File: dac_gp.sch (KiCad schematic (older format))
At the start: 7 parts, among them U17 MAX5802

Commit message: cleanup from Eagle import
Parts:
- C52, C53: footprint adc_dac_v1:C0603 -> Capacitor_SMD:C_0603_1608Metric; symbol adc_dac_v1-eagle-import:C-USC0603 -> Device:C
- R33, R34, R35, R36: footprint adc_dac_v1:R0603 -> Resistor_SMD:R_0603_1608Metric; symbol adc_dac_v1-eagle-import:R-US_R0603 -> Device:R_US
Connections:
- net labels added: +3V3, +5V
- net labels removed: 3V3, 5V
- wire segments 21 -> 25
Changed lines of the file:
@@
 $Descr User 12505 8268
 encoding utf-8
-Sheet 12 14
+Sheet 6 8
 Title ""
 Date ""
@@
 Comment4 ""
 $EndDescr
-Wire Wire Line
-	6000 2500 5500 2500
-Text GLabel 5500 2500 2    70   BiDi ~ 0
-3V3
-Wire Wire Line
-	4200 2400 4200 2200
-Wire Wire Line
-	4200 2200 4500 2200
-Wire Wire Line
-	4500 2200 4800 2200
-Wire Wire Line
-	4500 2300 4500 2200
-Connection ~ 4500 2200
-Text GLabel 4200 2200 2    70   BiDi ~ 0
-3V3
-Wire Wire Line
-	5000 1500 5000 1300
-Text GLabel 5000 1400 2    70   BiDi ~ 0
-3V3
-Wire Wire Line
-	6000 2300 5500 2300
-Text GLabel 5500 2300 2    70   BiDi ~ 0
-5V_REF
-Wire Wire Line
-	7900 2700 8200 2700
-Wire Wire Line
-	8200 2700 8200 2900
-Text GLabel 7900 2700 0    10   BiDi ~ 0
-GND
-Wire Wire Line
-	5800 3500 5800 3400
-Text GLabel 5800 3500 0    10   BiDi ~ 0
-GND
-Wire Wire Line
-	5000 1800 5000 1900
-Text GLabel 5000 1800 0    10   BiDi ~ 0
-GND
-Wire Wire Line
-	5400 1900 5400 1800
-Text GLabel 5400 1900 0    10   BiDi ~ 0
-GND
-Wire Wire Line
-	6000 2400 5500 2400
-Text GLabel 5500 2400 2    70   BiDi ~ 0
-5V
-Wire Wire Line
-	5400 1300 5400 1500
-Text GLabel 5400 1400 2    70   BiDi ~ 0
-5V
-Wire Wire Line
-	7900 2300 8300 2300
-Text GLabel 8000 2300 2    70   BiDi ~ 0
-DS_OUT0
-Wire Wire Line
-	7900 2400 8300 2400
-Text GLabel 8000 2400 2    70   BiDi ~ 0
-DS_OUT1
-Wire Wire Line
-	4800 2600 6000 2600
-Text GLabel 5500 2600 2    70   BiDi ~ 0
-DS_SDA
-Wire Wire Line
-	4500 2700 6000 2700
-Text GLabel 5500 2700 2    70   BiDi ~ 0
-DS_SCL
-Wire Wire Line
-	6000 2800 4200 2800
-Text GLabel 5400 2800 2    70   BiDi ~ 0
-DS_CLRB
-Wire Wire Line
-	5800 3000 5800 2900
-Wire Wire Line
-	5800 2900 6000 2900
 $Comp
 L adc_dac_v1-eagle-import:FRAME_A_L #FRAME7
@@
 $EndComp
 $Comp
-L adc_dac_v1-eagle-import:FRAME_A_L #FRAME7
-U 2 1 519C2D19
-P 7700 6900
-F 0 "#FRAME7" H 7700 6900 50  0001 C CNN
-F 1 "FRAME_A_L" H 7700 6900 50  0001 C CNN
-F 2 "" H 7700 6900 50  0001 C CNN
-F 3 "" H 7700 6900 50  0001 C CNN
-	2    7700 6900
-	1    0    0    -1
-$EndComp
-$Comp
-L adc_dac_v1-eagle-import:GND #GND63
+L power:GND #GND063
 U 1 1 E9B71633
 P 8200 3000
-F 0 "#GND63" H 8200 3000 50  0001 C CNN
+F 0 "#GND063" H 8200 3000 50  0001 C CNN
 F 1 "GND" H 8100 2900 59  0000 L BNN
 F 2 "" H 8200 3000 50  0001 C CNN
@@
 $EndComp
 $Comp
-L adc_dac_v1-eagle-import:R-US_R0603 R33
+L Device:R_US R33
 U 1 1 FACA8B8B
 P 4800 2400
 F 0 "R33" H 4650 2459 59  0000 L BNN
 F 1 "4.7k" H 4650 2270 59  0000 L BNN
-F 2 "adc_dac_v1:R0603" H 4800 2400 50  0001 C CNN
+F 2 "Resistor_SMD:R_0603_1608Metric" H 4800 2400 50  0001 C CNN
 F 3 "" H 4800 2400 50  0001 C CNN
 	1    4800 2400
-	0    -1   -1   0
-$EndComp
-$Comp
-L adc_dac_v1-eagle-import:R-US_R0603 R34
+	1    0    0    -1
+$EndComp
+$Comp
+L Device:R_US R34
 U 1 1 24585AD3
 P 4500 2500
 F 0 "R34" H 4350 2559 59  0000 L BNN
 F 1 "4.7k" H 4350 2370 59  0000 L BNN
-F 2 "adc_dac_v1:R0603" H 4500 2500 50  0001 C CNN
+F 2 "Resistor_SMD:R_0603_1608Metric" H 4500 2500 50  0001 C CNN
 F 3 "" H 4500 2500 50  0001 C CNN
 	1    4500 2500
-	0    -1   -1   0
-$EndComp
-$Comp
-L adc_dac_v1-eagle-import:R-US_R0603 R35
+	1    0    0    -1
+$EndComp
+$Comp
+L Device:R_US R35
 U 1 1 8E3E5586
 P 4200 2600
 F 0 "R35" H 4050 2659 59  0000 L BNN
 F 1 "100k" H 4050 2470 59  0000 L BNN
-F 2 "adc_dac_v1:R0603" H 4200 2600 50  0001 C CNN
+F 2 "Resistor_SMD:R_0603_1608Metric" H 4200 2600 50  0001 C CNN
 F 3 "" H 4200 2600 50  0001 C CNN
 	1    4200 2600
-	0    -1   -1   0
-$EndComp
-$Comp
-L adc_dac_v1-eagle-import:R-US_R0603 R36
+	1    0    0    -1
+$EndComp
+$Comp
+L Device:R_US R36
 U 1 1 610F8BED
 P 5800 3200
 F 0 "R36" H 5650 3259 59  0000 L BNN
 F 1 "100k" H 5650 3070 59  0000 L BNN
-F 2 "adc_dac_v1:R0603" H 5800 3200 50  0001 C CNN
+F 2 "Resistor_SMD:R_0603_1608Metric" H 5800 3200 50  0001 C CNN
 F 3 "" H 5800 3200 50  0001 C CNN
 	1    5800 3200
-	0    -1   -1   0
-$EndComp
-$Comp
-L adc_dac_v1-eagle-import:GND #GND64
+	1    0    0    -1
+$EndComp
+$Comp
+L power:GND #GND064
 U 1 1 C02F8759
 P 5800 3600
-F 0 "#GND64" H 5800 3600 50  0001 C CNN
+F 0 "#GND064" H 5800 3600 50  0001 C CNN
 F 1 "GND" H 5700 3500 59  0000 L BNN
 F 2 "" H 5800 3600 50  0001 C CNN
@@
 $EndComp
 $Comp
-L adc_dac_v1-eagle-import:C-USC0603 C52
+L Device:C C52
 U 1 1 A7A1DCDA
-P 5000 1600
-F 0 "C52" H 5040 1625 59  0000 L BNN
-F 1 "0.1u" H 5040 1435 59  0000 L BNN
-F 2 "adc_dac_v1:C0603" H 5000 1600 50  0001 C CNN
-F 3 "" H 5000 1600 50  0001 C CNN
-	1    5000 1600
-	1    0    0    -1
-$EndComp
-$Comp
-L adc_dac_v1-eagle-import:C-USC0603 C53
+P 5000 1700
+F 0 "C52" H 5040 1725 59  0000 L BNN
+F 1 "0.1u" H 5040 1535 59  0000 L BNN
+F 2 "Capacitor_SMD:C_0603_1608Metric" H 5000 1700 50  0001 C CNN
+F 3 "" H 5000 1700 50  0001 C CNN
+	1    5000 1700
+	1    0    0    -1
+$EndComp
+$Comp
+L Device:C C53
 U 1 1 46ACB443
-P 5400 1600
-F 0 "C53" H 5440 1625 59  0000 L BNN
-F 1 "0.1u" H 5440 1435 59  0000 L BNN
-F 2 "adc_dac_v1:C0603" H 5400 1600 50  0001 C CNN
-F 3 "" H 5400 1600 50  0001 C CNN
-	1    5400 1600
-	1    0    0    -1
-$EndComp
-$Comp
-L adc_dac_v1-eagle-import:GND #GND62
+P 5400 1650
+F 0 "C53" H 5440 1675 59  0000 L BNN
+F 1 "0.1u" H 5440 1485 59  0000 L BNN
+F 2 "Capacitor_SMD:C_0603_1608Metric" H 5400 1650 50  0001 C CNN
+F 3 "" H 5400 1650 50  0001 C CNN
+	1    5400 1650
+	1    0    0    -1
+$EndComp
+$Comp
+L power:GND #GND062
 U 1 1 FC55E54D
 P 5000 2000
-F 0 "#GND62" H 5000 2000 50  0001 C CNN
+F 0 "#GND062" H 5000 2000 50  0001 C CNN
 F 1 "GND" H 4900 1900 59  0000 L BNN
 F 2 "" H 5000 2000 50  0001 C CNN
@@
 $EndComp
 $Comp
-L adc_dac_v1-eagle-import:GND #GND80
+L power:GND #GND080
 U 1 1 10B103BF
 P 5400 2000
-F 0 "#GND80" H 5400 2000 50  0001 C CNN
+F 0 "#GND080" H 5400 2000 50  0001 C CNN
 F 1 "GND" H 5300 1900 59  0000 L BNN
 F 2 "" H 5400 2000 50  0001 C CNN
@@
 	1    0    0    -1
 $EndComp
+Text GLabel 5500 2300 2    70   BiDi ~ 0
+5V_REF
+Text GLabel 8150 2300 2    70   BiDi ~ 0
+DS_OUT0
+Text GLabel 8150 2400 2    70   BiDi ~ 0
+DS_OUT1
+Text GLabel 5500 2600 2    70   BiDi ~ 0
+DS_SDA
+Text GLabel 5500 2700 2    70   BiDi ~ 0
+DS_SCL
+Text GLabel 5400 2800 2    70   BiDi ~ 0
+DS_CLRB
 Text Notes 6300 3200 0    59   ~ 0
 Slow DAC for offset voltages, etc.
+Wire Wire Line
+	6000 2500 5500 2500
+Wire Wire Line
+	4500 2200 4800 2200
+Wire Wire Line
+	6000 2300 5500 2300
+Wire Wire Line
+	7900 2700 8200 2700
+Wire Wire Line
+	6000 2400 5500 2400
+Wire Wire Line
+	5400 1300 5400 1500
+Wire Wire Line
+	7900 2300 8150 2300
+Wire Wire Line
+	7900 2400 8150 2400
+Wire Wire Line
+	4800 2600 6000 2600
+Wire Wire Line
+	4500 2700 6000 2700
+Wire Wire Line
+	6000 2800 4200 2800
+Wire Wire Line
+	5800 2900 6000 2900
+Connection ~ 4500 2200
+Wire Wire Line
+	5400 1800 5400 2000
+Wire Wire Line
+	5800 2900 5800 3050
+Wire Wire Line
+	5800 3350 5800 3600
+Wire Wire Line
+	4200 2800 4200 2750
+Wire Wire Line
+	4200 2200 4200 2450
+Wire Wire Line
+	4500 2200 4500 2350
+Wire Wire Line
+	4500 2650 4500 2700
+Wire Wire Line
+	4800 2600 4800 2550
+Wire Wire Line
+	4800 2250 4800 2200
+Wire Wire Line
+	5000 1350 5000 1550
+Wire Wire Line
+	5000 2000 5000 1850
+Wire Wire Line
+	8200 2700 8200 3000
+$Comp
+L power:+5V #PWR0123
+U 1 1 61889133
+P 5400 1300
+F 0 "#PWR0123" H 5400 1150 50  0001 C CNN
+F 1 "+5V" H 5415 1473 50  0000 C CNN
+F 2 "" H 5400 1300 50  0001 C CNN
+F 3 "" H 5400 1300 50  0001 C CNN
+	1    5400 1300
+	1    0    0    -1
+$EndComp
+$Comp
+L power:+5V #PWR0124
+U 1 1 6188A365
+P 5500 2400
+F 0 "#PWR0124" H 5500 2250 50  0001 C CNN
+F 1 "+5V" V 5515 2528 50  0000 L CNN
+F 2 "" H 5500 2400 50  0001 C CNN
+F 3 "" H 5500 2400 50  0001 C CNN
+	1    5500 2400
+	0    -1   -1   0
+$EndComp
+$Comp
+L power:+3V3 #PWR0125
+U 1 1 6188B164
+P 5000 1350
+F 0 "#PWR0125" H 5000 1200 50  0001 C CNN
+F 1 "+3V3" H 5015 1523 50  0000 C CNN
+F 2 "" H 5000 1350 50  0001 C CNN
+F 3 "" H 5000 1350 50  0001 C CNN
+	1    5000 1350
+	1    0    0    -1
+$EndComp
+$Comp
+L power:+3V3 #PWR0126
+U 1 1 6188C0A8
+P 4500 2200
+F 0 "#PWR0126" H 4500 2050 50  0001 C CNN
+F 1 "+3V3" H 4515 2373 50  0000 C CNN
+F 2 "" H 4500 2200 50  0001 C CNN
+F 3 "" H 4500 2200 50  0001 C CNN
+	1    4500 2200
+	1    0    0    -1
+$EndComp
+$Comp
+L power:+3V3 #PWR0127
+U 1 1 6188C619
+P 5500 2500
+F 0 "#PWR0127" H 5500 2350 50  0001 C CNN
+F 1 "+3V3" V 5515 2628 50  0000 L CNN
+F 2 "" H 5500 2500 50  0001 C CNN
+F 3 "" H 5500 2500 50  0001 C CNN
+	1    5500 2500
+	0    -1   -1   0
+$EndComp
+Wire Wire Line
+	4200 2200 4500 2200
 $EndSCHEMATC

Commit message: added different general purpose ADC
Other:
- note added: "Slow DAC for offset voltages, etc.\n This Maxim part is now hard to find. \n\nConsidering instead the TI DAC53401"
- note removed: "Slow DAC for offset voltages, etc."
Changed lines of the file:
@@
 Text GLabel 5400 2800 2    70   BiDi ~ 0
 DS_CLRB
-Text Notes 6300 3200 0    59   ~ 0
-Slow DAC for offset voltages, etc.
+Text Notes 6200 3450 0    59   ~ 0
+Slow DAC for offset voltages, etc.\n This Maxim part is now hard to find. \n\nConsidering instead the TI DAC53401
 Wire Wire Line
 	6000 2500 5500 2500

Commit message: edits to general purpose DAC and gp ADC
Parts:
- removed R33, R34: 4.7k, Resistor_SMD:R_0603_1608Metric, symbol Device:R_US
- removed R35, R36: 100k, Resistor_SMD:R_0603_1608Metric, symbol Device:R_US
- removed U17: MAX5802, adc_dac_v1:21-0061L_MXM, symbol adc_dac_v1-eagle-import:MAX5802BAUB+
- added R?: 0, Resistor_SMD:R_0603_1608Metric, symbol Device:R_US
- added U?: DAC80508ZRTER, RTE0016D, symbol covg-kicad:DAC80508ZRTER
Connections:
- net labels added: CSB, OUT0, OUT1, OUT2, OUT3, OUT4, OUT5, OUT6, OUT7, OUT[0..7], SCLK, SDI, SDO
- net labels removed: 5V_REF, DS_CLRB, DS_OUT0, DS_OUT1, DS_SCL, DS_SDA
- wire segments 25 -> 22
- no-connect marks 0 -> 1
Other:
- note added: "Add connector here?"
- note added: "Howland Current Source (needs to MUX to any DAC HDMI signal)"
- note added: "Optional gain and unipolar to bipolar"
- note added: "Use internal reference\n\nbring out just in case."
- note removed: "Slow DAC for offset voltages, etc.\n This Maxim part is now hard to find. \n\nConsidering instead the TI DAC53401"
- moved on the sheet: C52, C53

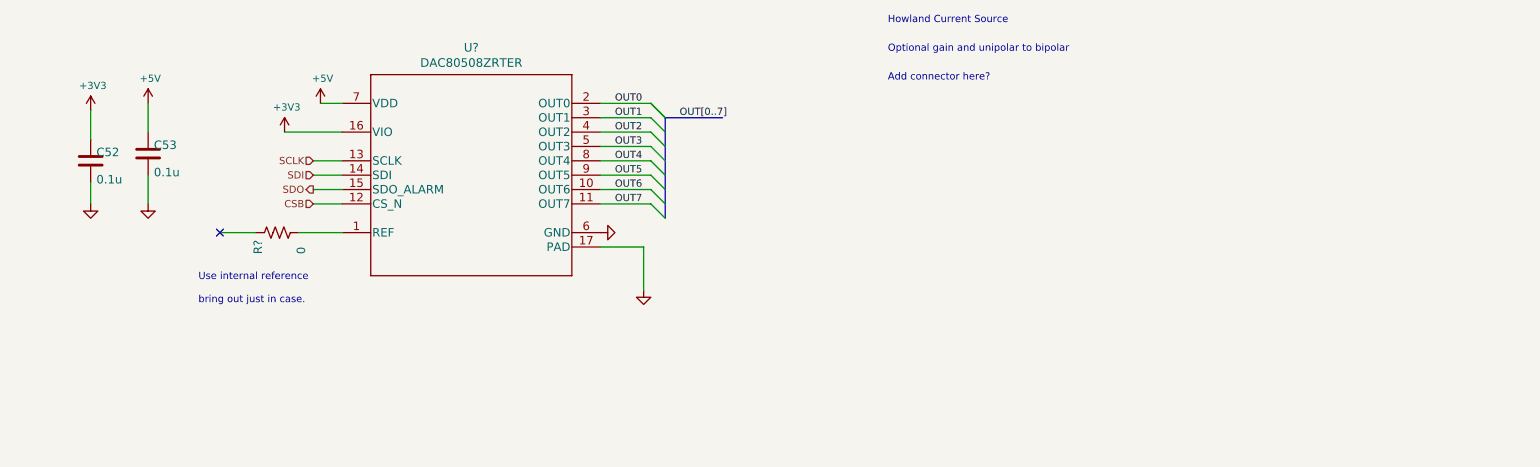
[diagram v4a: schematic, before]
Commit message: completed fast ADC and DAC; start on gp DAC
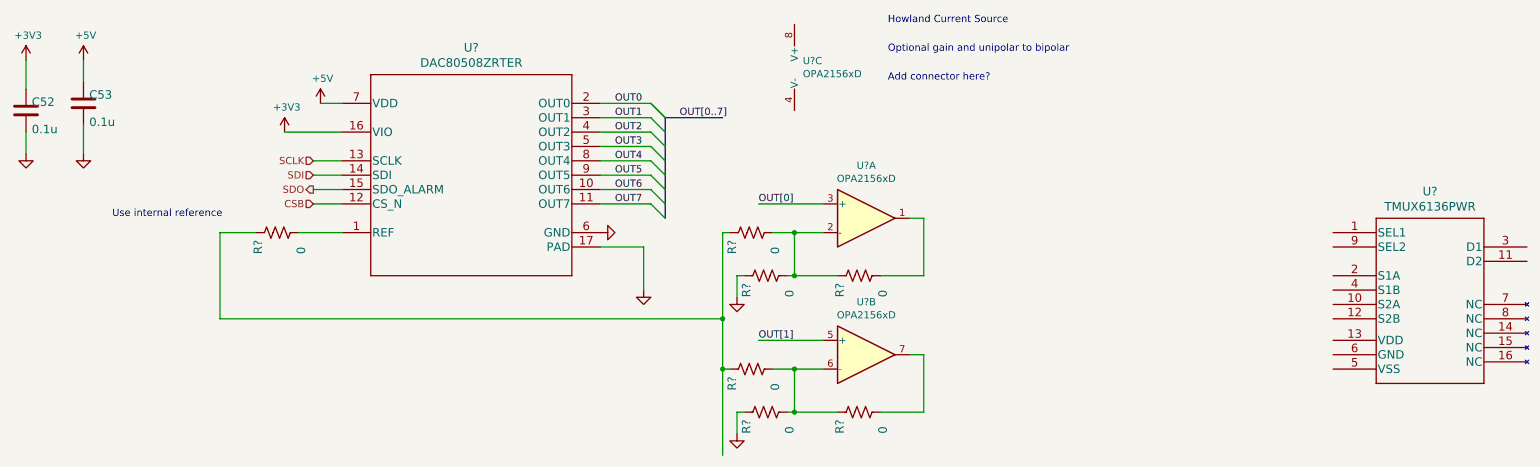
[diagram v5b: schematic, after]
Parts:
- added R? (x6): 0, Resistor_SMD:R_0603_1608Metric, symbol Device:R_US
- added U? (x3): OPA2156xD, Package_SO:SOIC-8_3.9x4.9mm_P1.27mm, symbol Amplifier_Operational:OPA2156xD
- added U?: TMUX6136PWR, PW16_TEX, symbol covg-kicad:TMUX6136PWR
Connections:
- net GND: now also R?.1, R?.1
- net at R?.1: now also R?.1, R?.1
- new net: R?.2, U?.1
- new net: R?.1, R?.2, R?.2, U?.2 (-)
- new net: R?.1, R?.2, R?.2, U?.6 (-)
- new net: R?.2, U?.7
- new net OUT[0]: U?.3 (+)
- new net OUT[1]: U?.5 (+)
- no-connect marks 1 -> 0
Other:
- note added: "Use internal reference \n 0.1 Ohm output impedance"
- note removed: "Use internal reference\n\nbring out just in case."
- moved on the sheet: C52, C53
